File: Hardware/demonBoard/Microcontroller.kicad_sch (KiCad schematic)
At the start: 30 parts, among them J1 TYPE-C-31-M-12, J2 UART_CONN, U1 USBLC6-2SC6, U2 SPX3819M5-L-3-3, U3 ESP32-C3-WROOM-02

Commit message: doc: Add schematic pdf
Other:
- company: (none) -> Vagarth Gaurav
- title: (none) -> Demon board
- moved on the sheet: C1, C2, C3, C4, C5, C6, C7, C8, C9, D1, D2, D3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

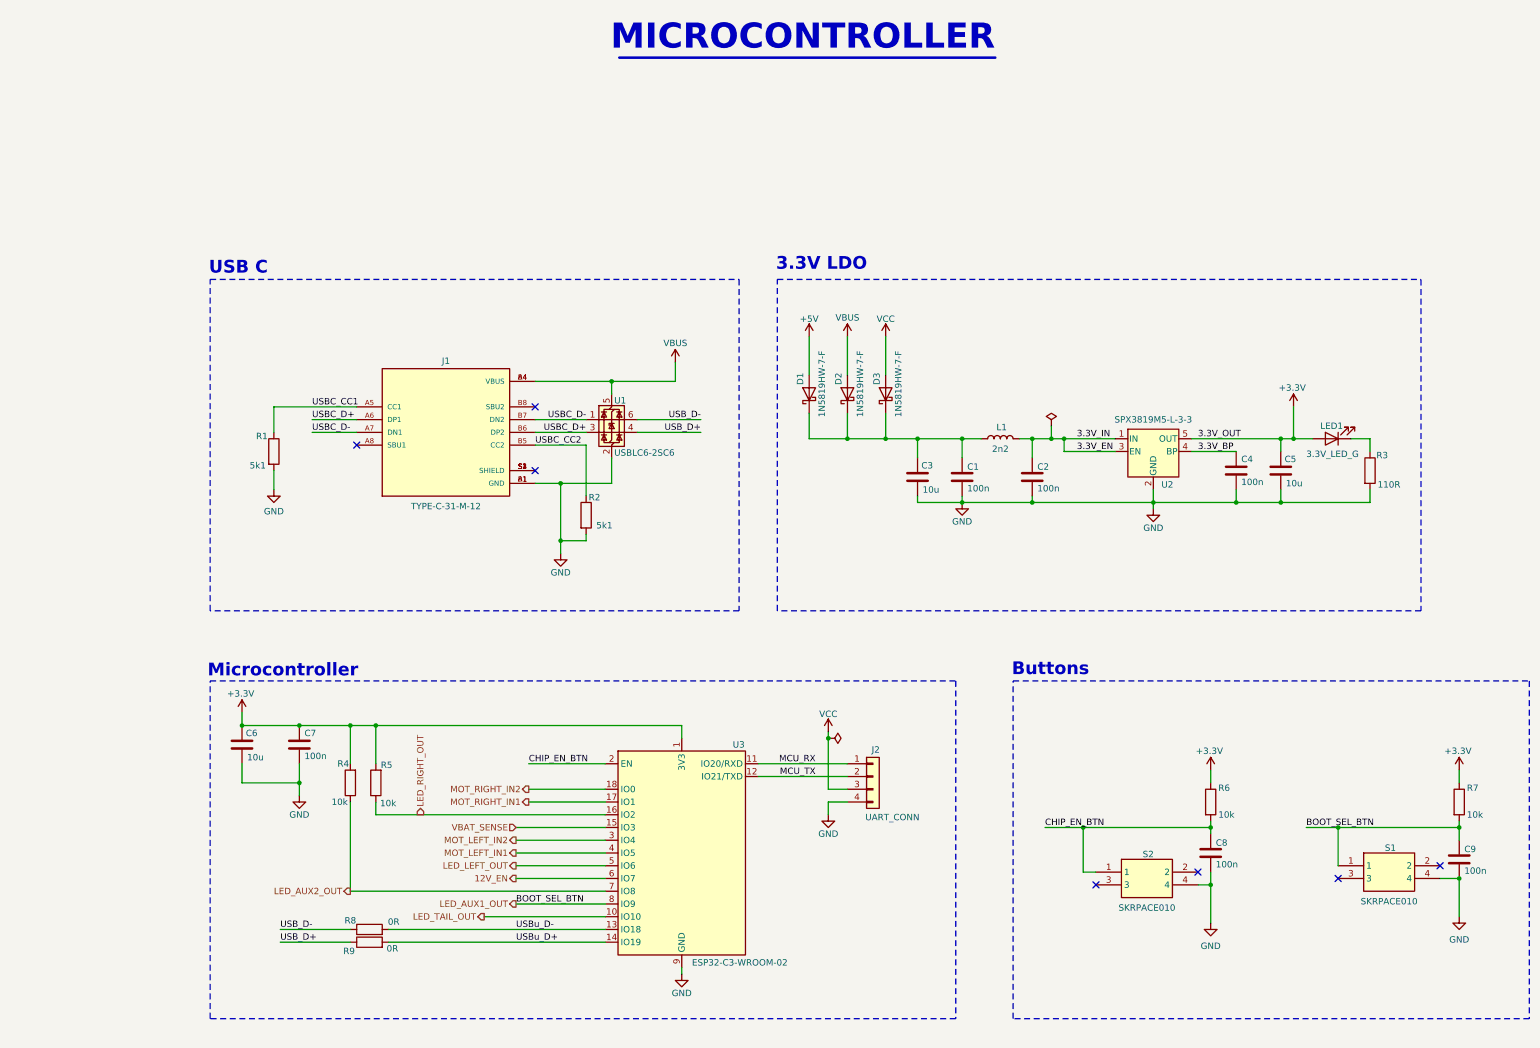
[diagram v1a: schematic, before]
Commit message: Change resistors for leds
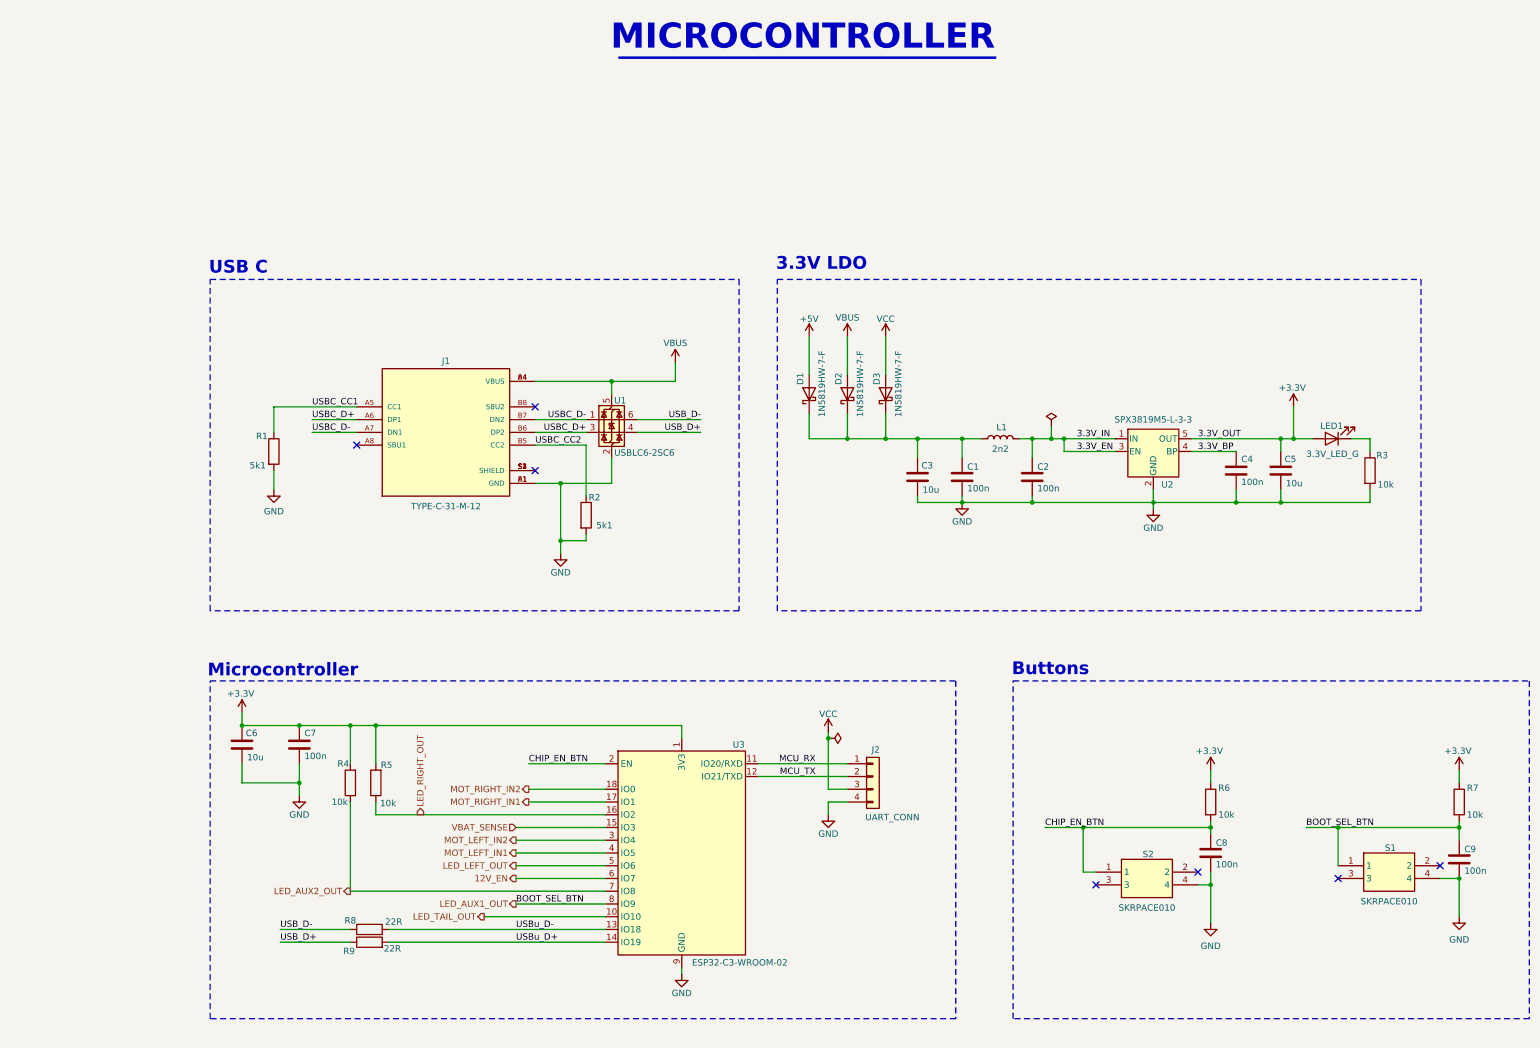
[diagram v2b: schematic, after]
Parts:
- R3: value 110R -> 10k
- R8, R9: value 0R -> 22R
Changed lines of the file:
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@@
 			)
 		)
-		(property "Value" "110R"
+		(property "Value" "10k"
 			(at 325.374 106.934 0)
 			(effects
@@
 			)
 		)
-		(property "Value" "0R"
+		(property "Value" "22R"
 			(at 129.032 199.39 90)
 			(effects
@@
 			)
 		)
-		(property "Value" "0R"
+		(property "Value" "22R"
 			(at 129.286 194.056 90)
 			(effects
